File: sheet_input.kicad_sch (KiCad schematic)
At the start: 45 parts, among them J1 NCJ6FA-H, J5 VDD_PoE / PGND, K1 KAQY214S, K2 KAQY214S, Q1 DMP3098 (P-FET 60V), SW1 SS-12D00-G3, U3 TLV9061, U4 74HC4053

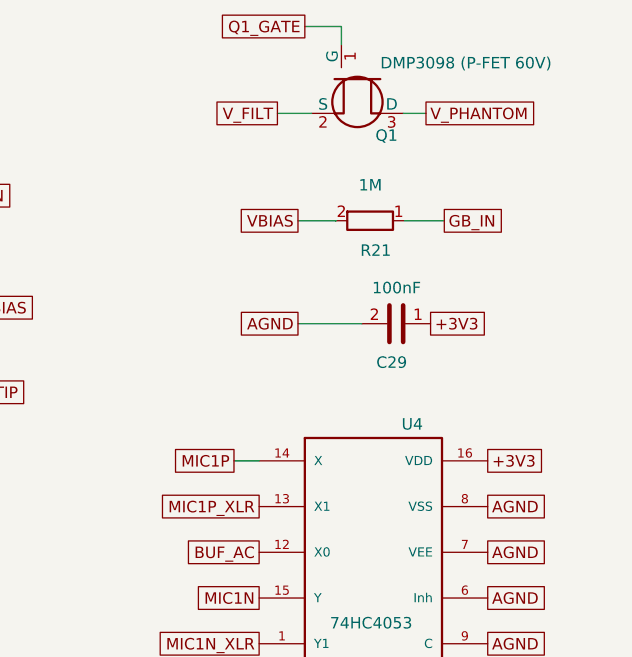
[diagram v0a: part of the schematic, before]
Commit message: input: J7 1x4 socket for direct eurorack-module coupling (alt to J1) + R27 0R instrument-mode jumper, both DNP
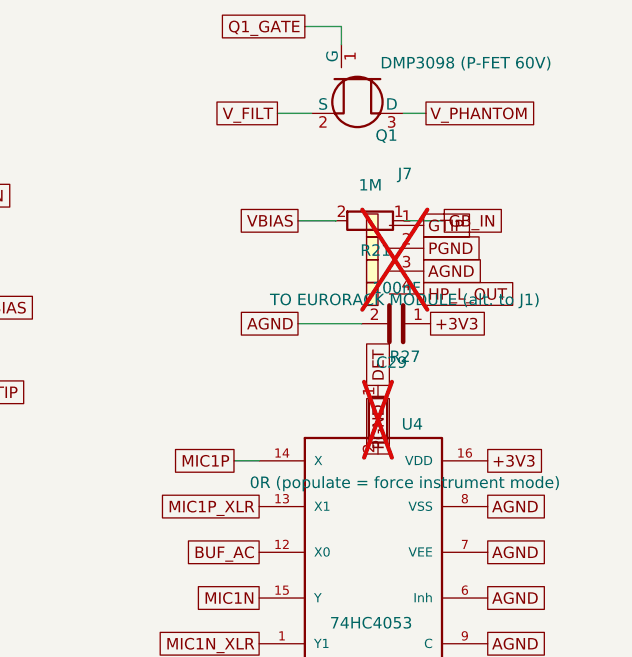
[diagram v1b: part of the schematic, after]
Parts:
- added J7: TO EURORACK MODULE (alt. to J1), Connector_PinSocket_2.54mm:PinSocket_1x04_P2.54mm_Vertical, symbol scramble_hat:Conn_01x04
- added R27: 0R (populate = force instrument mode), Resistor_SMD:R_0805_2012Metric, symbol scramble_hat:R
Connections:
- net AGND: now also J7.3 (Pin_3)
- net DET: now also R27.1
- net GTIP: now also J7.1 (Pin_1)
- net PGND: now also J7.2 (Pin_2), R27.2
- new net HP_L_OUT: J7.4 (Pin_4)
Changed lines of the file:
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@@
 		(comment 1 "Chunk 2: Neutrik combo input + ESD + isolated phantom block + isolation barrier + status LED")
+	)
+		(symbol
+			(lib_id "scramble_hat:Conn_01x04")
+			(at 355.6 149.86 0)
+			(unit 1)
+			(exclude_from_sim no)
+			(in_bom yes)
+			(on_board yes)
+			(dnp yes)
+			(property "Reference" "J7"
+				(at 358.6 142.86 0)
+				(show_name no)
+				(do_not_autoplace no)
+				(effects (font (size 1.27 1.27)))
+			)
+			(property "Value" "TO EURORACK MODULE (alt. to J1)"
+				(at 358.6 156.86 0)
+				(show_name no)
+				(do_not_autoplace no)
+				(effects (font (size 1.27 1.27)))
+			)
+			(property "Footprint" "Connector_PinSocket_2.54mm:PinSocket_1x04_P2.54mm_Vertical"
+				(at 355.6 149.86 0)
+				(show_name no)
+				(do_not_autoplace no)
+				(hide yes)
+				(effects (font (size 1.27 1.27)))
+			)
+			(property "Datasheet" ""
+				(at 355.6 149.86 0)
+				(show_name no)
+				(do_not_autoplace no)
+				(hide yes)
+				(effects (font (size 1.27 1.27)))
+			)
+			(property "Description" ""
+				(at 355.6 149.86 0)
+				(show_name no)
+				(do_not_autoplace no)
+				(hide yes)
+				(effects (font (size 1.27 1.27)))
+			)
+			(pin "1"
+			)
+			(pin "2"
+			)
+			(pin "3"
+			)
+			(pin "4"
+			)
+			(instances
+				(project "scramble_hat"
+					(path "/2b93e89d-bdf9-4578-8fa1-59d0c819a910/f89707d4-5ec9-426f-a042-e33ce0e25fbe"
+						(reference "J7")
+						(unit 1)
+					)
+				)
+			)
+		)
+		(symbol
+			(lib_id "scramble_hat:R")
+			(at 355.6 170.18 0)
+			(unit 1)
+			(exclude_from_sim no)
+			(in_bom yes)
+			(on_board yes)
+			(dnp yes)
+			(property "Reference" "R27"
+				(at 358.6 163.18 0)
+				(show_name no)
+				(do_not_autoplace no)
+				(effects (font (size 1.27 1.27)))
+			)
+			(property "Value" "0R (populate = force instrument mode)"
+				(at 358.6 177.18 0)
+				(show_name no)
+				(do_not_autoplace no)
+				(effects (font (size 1.27 1.27)))
+			)
+			(property "Footprint" "Resistor_SMD:R_0805_2012Metric"
+				(at 355.6 170.18 0)
+				(show_name no)
+				(do_not_autoplace no)
+				(hide yes)
+				(effects (font (size 1.27 1.27)))
+			)
+			(property "Datasheet" ""
+				(at 355.6 170.18 0)
+				(show_name no)
+				(do_not_autoplace no)
+				(hide yes)
+				(effects (font (size 1.27 1.27)))
+			)
+			(property "Description" ""
+				(at 355.6 170.18 0)
+				(show_name no)
+				(do_not_autoplace no)
+				(hide yes)
+				(effects (font (size 1.27 1.27)))
+			)
+			(pin "1"
+			)
+			(pin "2"
+			)
+			(instances
+				(project "scramble_hat"
+					(path "/2b93e89d-bdf9-4578-8fa1-59d0c819a910/f89707d4-5ec9-426f-a042-e33ce0e25fbe"
+						(reference "R27")
+						(unit 1)
+					)
+				)
+			)
+		)
+	(global_label "GTIP"
+		(shape passive)
+		(at 360.68 148.59 0)
+		(effects
+			(font
+				(size 1.27 1.27)
+			)
+			(justify left)
+		)
+		(property "Intersheetrefs" "${INTERSHEET_REFS}"
+			(at 360.68 148.59 0)
+			(hide yes)
+			(show_name no)
+			(do_not_autoplace no)
+			(effects
+				(font
+					(size 1.27 1.27)
+				)
+			)
+		)
+	)
+	(global_label "PGND"
+		(shape passive)
+		(at 360.68 151.13 0)
+		(effects
+			(font
+				(size 1.27 1.27)
+			)
+			(justify left)
+		)
+		(property "Intersheetrefs" "${INTERSHEET_REFS}"
+			(at 360.68 151.13 0)
+			(hide yes)
+			(show_name no)
+			(do_not_autoplace no)
+			(effects
+				(font
+					(size 1.27 1.27)
+				)
+			)
+		)
+	)
+	(global_label "AGND"
+		(shape passive)
+		(at 360.68 153.67 0)
+		(effects
+			(font
+				(size 1.27 1.27)
+			)
+			(justify left)
+		)
+		(property "Intersheetrefs" "${INTERSHEET_REFS}"
+			(at 360.68 153.67 0)
+			(hide yes)
+			(show_name no)
+			(do_not_autoplace no)
+			(effects
+				(font
+					(size 1.27 1.27)
+				)
+			)
+		)
+	)
+	(global_label "HP_L_OUT"
+		(shape passive)
+		(at 360.68 156.21 0)
+		(effects
+			(font
+				(size 1.27 1.27)
+			)
+			(justify left)
+		)
+		(property "Intersheetrefs" "${INTERSHEET_REFS}"
+			(at 360.68 156.21 0)
+			(hide yes)
+			(show_name no)
+			(do_not_autoplace no)
+			(effects
+				(font
+					(size 1.27 1.27)
+				)
+			)
+		)
+	)
+	(global_label "DET"
+		(shape passive)
+		(at 355.6 166.37 90)
+		(effects
+			(font
+				(size 1.27 1.27)
+			)
+			(justify left)
+		)
+		(property "Intersheetrefs" "${INTERSHEET_REFS}"
+			(at 355.6 166.37 90)
+			(hide yes)
+			(show_name no)
+			(do_not_autoplace no)
+			(effects
+				(font
+					(size 1.27 1.27)
+				)
+			)
+		)
+	)
+	(global_label "PGND"
+		(shape passive)
+		(at 355.6 173.99 270)
+		(effects
+			(font
+				(size 1.27 1.27)
+			)
+			(justify left)
+		)
+		(property "Intersheetrefs" "${INTERSHEET_REFS}"
+			(at 355.6 173.99 270)
+			(hide yes)
+			(show_name no)
+			(do_not_autoplace no)
+			(effects
+				(font
+					(size 1.27 1.27)
+				)
+			)
+		)
 	)
 	(wire

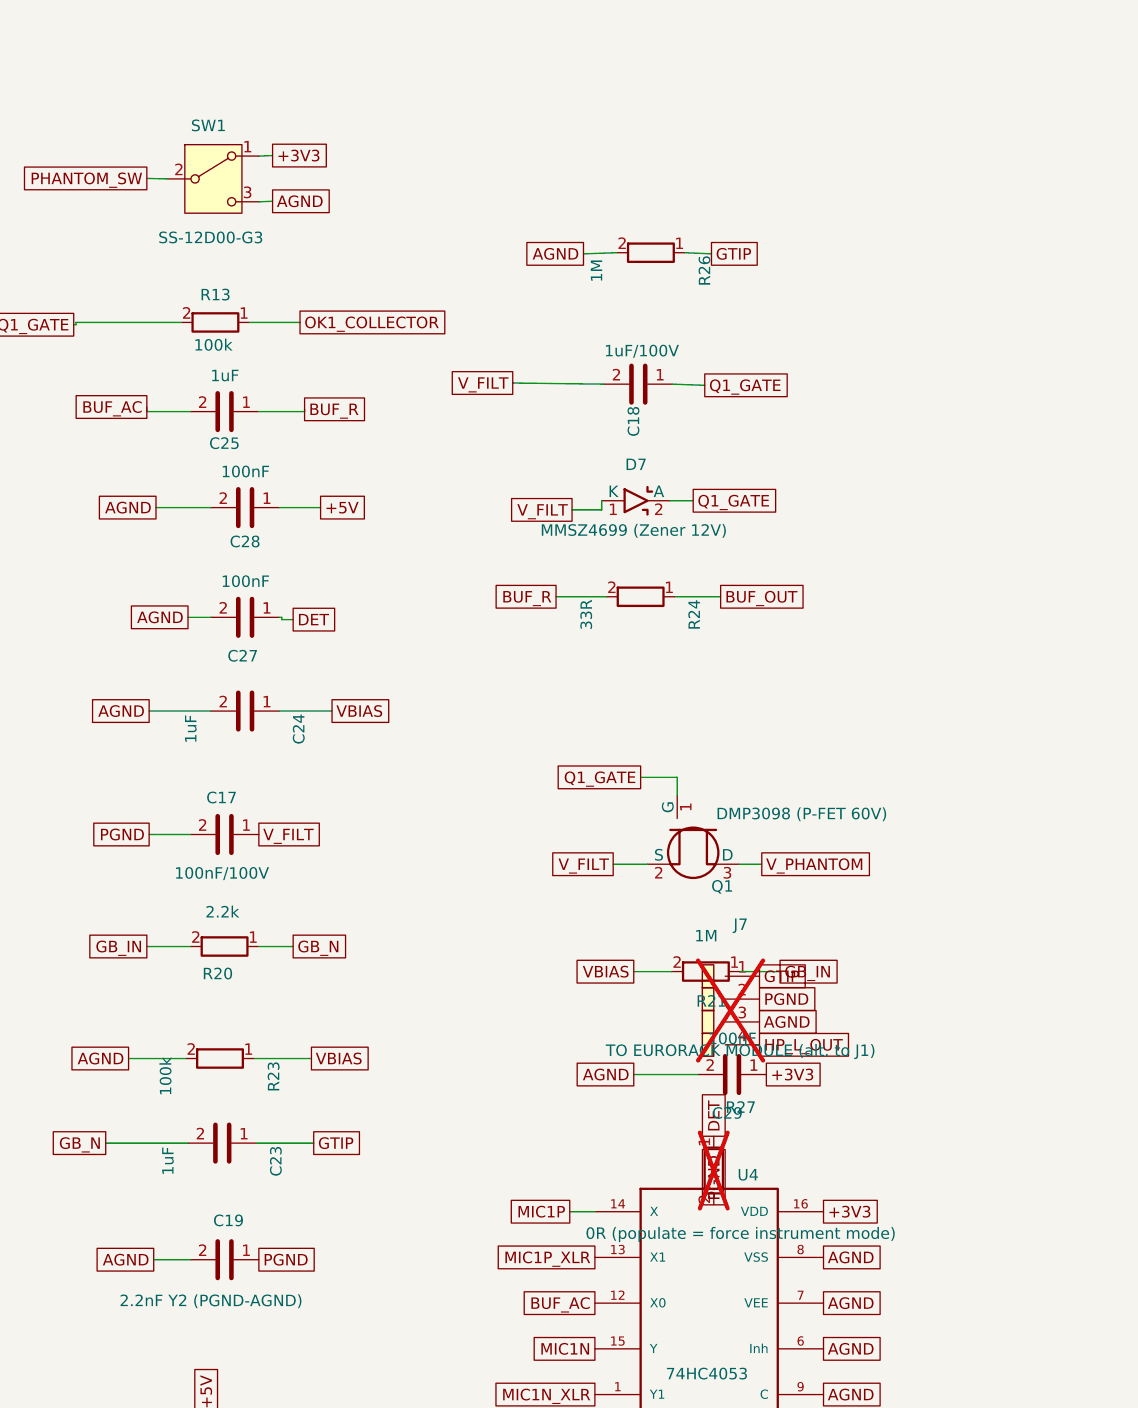
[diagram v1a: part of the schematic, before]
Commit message: sw1 optional: DNP by default (phantom-less builds); J7/R27 placed+routed; restore pos-file exclusions; regen fab + docs
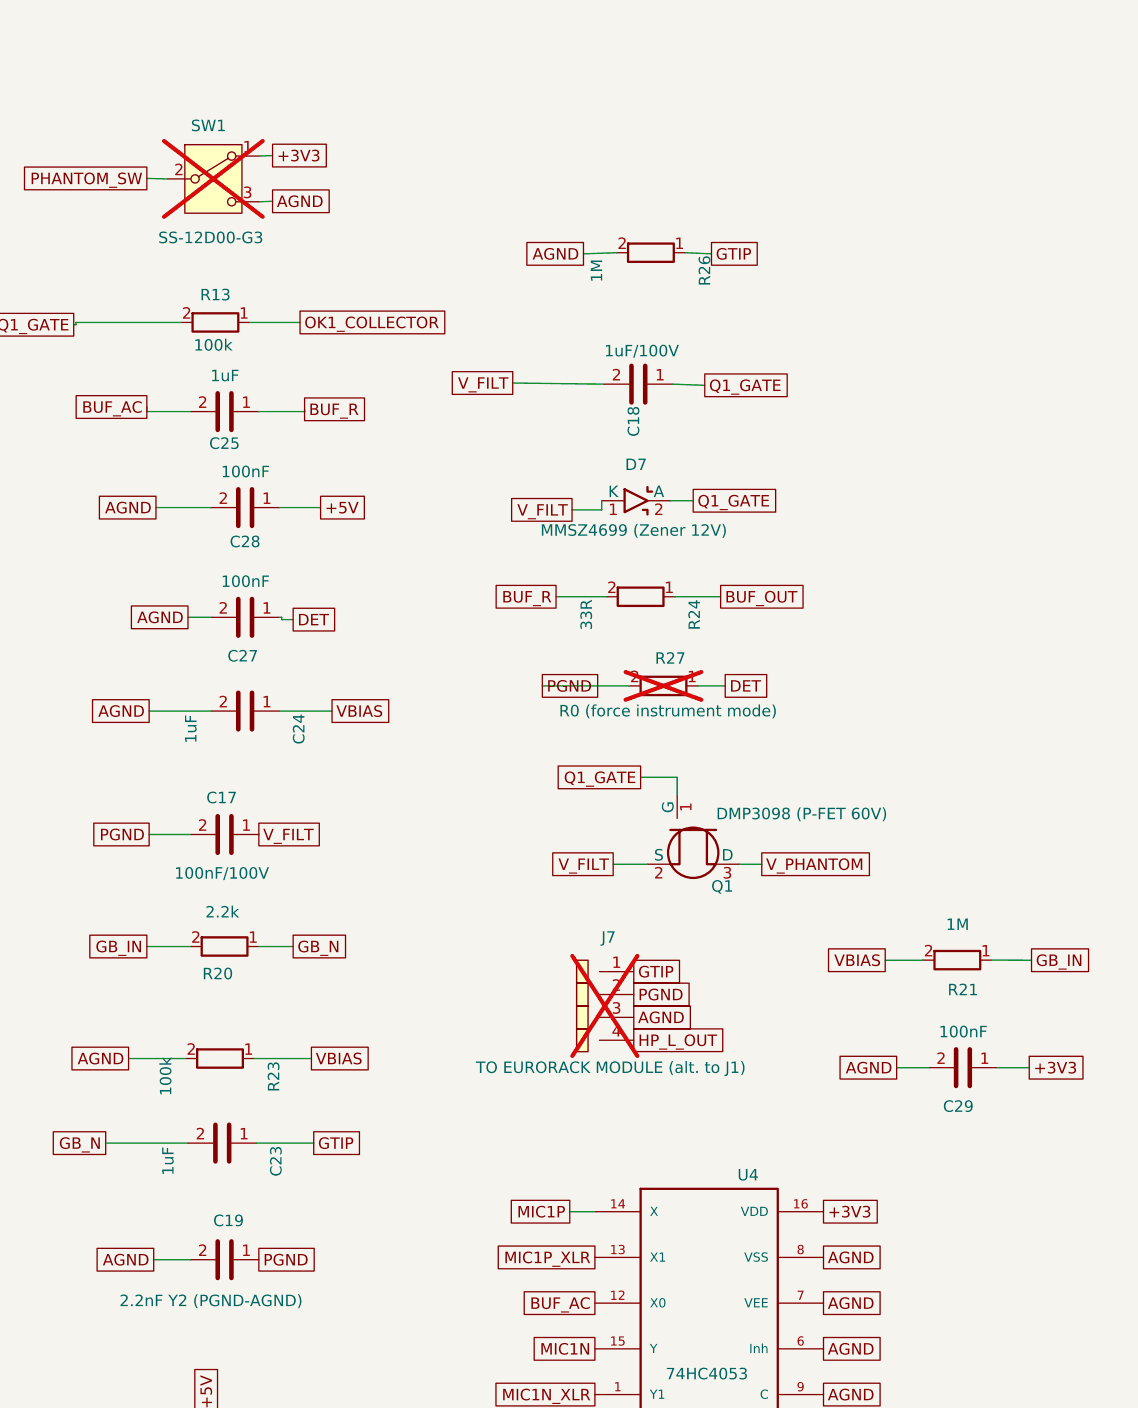
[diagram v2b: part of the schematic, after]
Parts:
- R27: value 0R (populate = force instrument mode) -> R0 (force instrument mode)
- SW1: now not fitted
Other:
- moved on the sheet: C29, J7, R21, R27

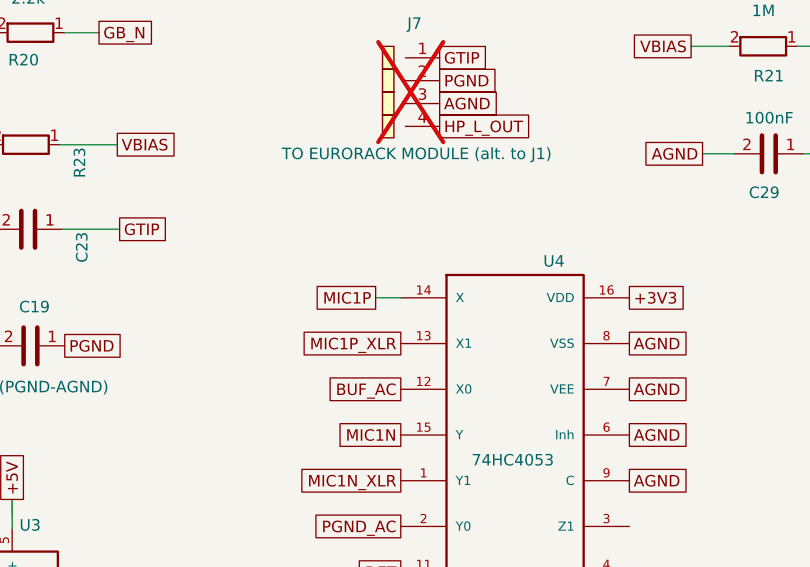
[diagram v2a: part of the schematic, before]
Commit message: input: C30 100nF/100V V_PHANTOM bypass at Q1 drain; BOM: datasheet links column, 6 stock-out swaps (OK1 -> EL3H7-VG, 5 resistors -> Yageo), price refresh
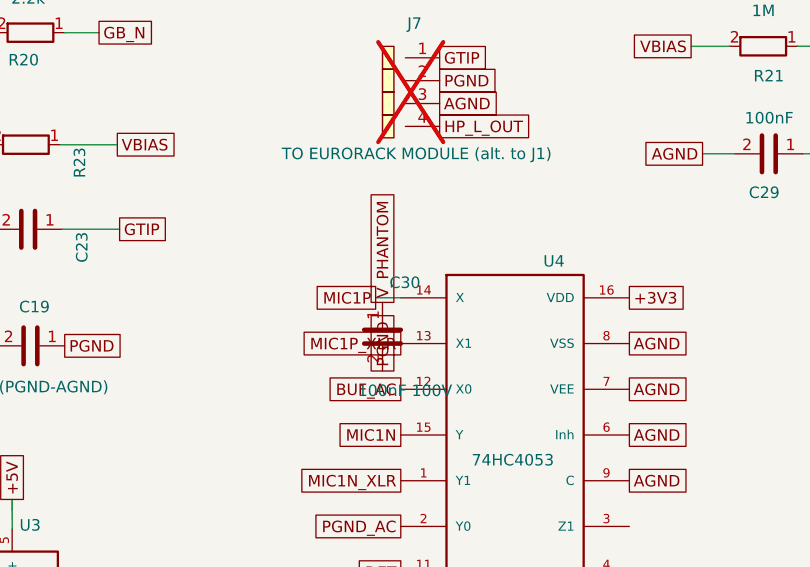
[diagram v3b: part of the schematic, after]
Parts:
- added C30: 100nF 100V, Capacitor_SMD:C_0805_2012Metric, symbol scramble_hat:C
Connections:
- net PGND: now also C30.2
- net V_PHANTOM: now also C30.1
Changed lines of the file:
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@@
 		(comment 1 "Chunk 2: Neutrik combo input + ESD + isolated phantom block + isolation barrier + status LED")
+	)
+		(symbol
+			(lib_id "scramble_hat:C")
+			(at 340.36 179.07 0)
+			(unit 1)
+			(exclude_from_sim no)
+			(in_bom yes)
+			(on_board yes)
+			(dnp no)
+			(property "Reference" "C30"
+				(at 342.86 173.07 0)
+				(show_name no)
+				(do_not_autoplace no)
+				(effects (font (size 1.27 1.27)))
+			)
+			(property "Value" "100nF 100V"
+				(at 342.86 185.07 0)
+				(show_name no)
+				(do_not_autoplace no)
+				(effects (font (size 1.27 1.27)))
+			)
+			(property "Footprint" "Capacitor_SMD:C_0805_2012Metric"
+				(at 340.36 179.07 0)
+				(show_name no)
+				(do_not_autoplace no)
+				(hide yes)
+				(effects (font (size 1.27 1.27)))
+			)
+			(property "Datasheet" "https://datasheet.lcsc.com/datasheet/pdf/9f6ef17093b8d551f8b17af0626ff758.pdf?productCode=C89258"
+				(at 340.36 179.07 0)
+				(show_name no)
+				(do_not_autoplace no)
+				(hide yes)
+				(effects (font (size 1.27 1.27)))
+			)
+			(property "Description" "V_PHANTOM bypass at Q1 drain (PoE hash filter)"
+				(at 340.36 179.07 0)
+				(show_name no)
+				(do_not_autoplace no)
+				(hide yes)
+				(effects (font (size 1.27 1.27)))
+			)
+			(pin "1"
+			)
+			(pin "2"
+			)
+			(instances
+				(project "scramble_hat"
+					(path "/2b93e89d-bdf9-4578-8fa1-59d0c819a910/f89707d4-5ec9-426f-a042-e33ce0e25fbe"
+						(reference "C30")
+						(unit 1)
+					)
+				)
+			)
+		)
+	(global_label "V_PHANTOM"
+		(shape passive)
+		(at 340.36 175.26 90)
+		(effects
+			(font
+				(size 1.27 1.27)
+			)
+			(justify left)
+		)
+		(property "Intersheetrefs" "${INTERSHEET_REFS}"
+			(at 340.36 175.26 90)
+			(hide yes)
+			(show_name no)
+			(do_not_autoplace no)
+			(effects
+				(font
+					(size 1.27 1.27)
+				)
+			)
+		)
+	)
+	(global_label "PGND"
+		(shape passive)
+		(at 340.36 182.88 270)
+		(effects
+			(font
+				(size 1.27 1.27)
+			)
+			(justify left)
+		)
+		(property "Intersheetrefs" "${INTERSHEET_REFS}"
+			(at 340.36 182.88 270)
+			(hide yes)
+			(show_name no)
+			(do_not_autoplace no)
+			(effects
+				(font
+					(size 1.27 1.27)
+				)
+			)
+		)
 	)
 	(wire
